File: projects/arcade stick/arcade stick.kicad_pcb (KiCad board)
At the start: 2 copper layers, 50 x 120 mm, 38 parts, among them SW1 SW_Push, SW10 SW_Push, SW11 SW_Push, SW12 SW_Push, SW13 SW_Push, SW14 SW_Push, SW15 SW_Push, SW16 SW_Push, SW2 SW_Push, SW3 SW_Push, SW4 SW_Push, SW5 SW_Push, SW6 SW_Push, SW7 SW_Push, SW8 SW_Push, SW9 SW_Push, U1 74HC165, U2 74HC165

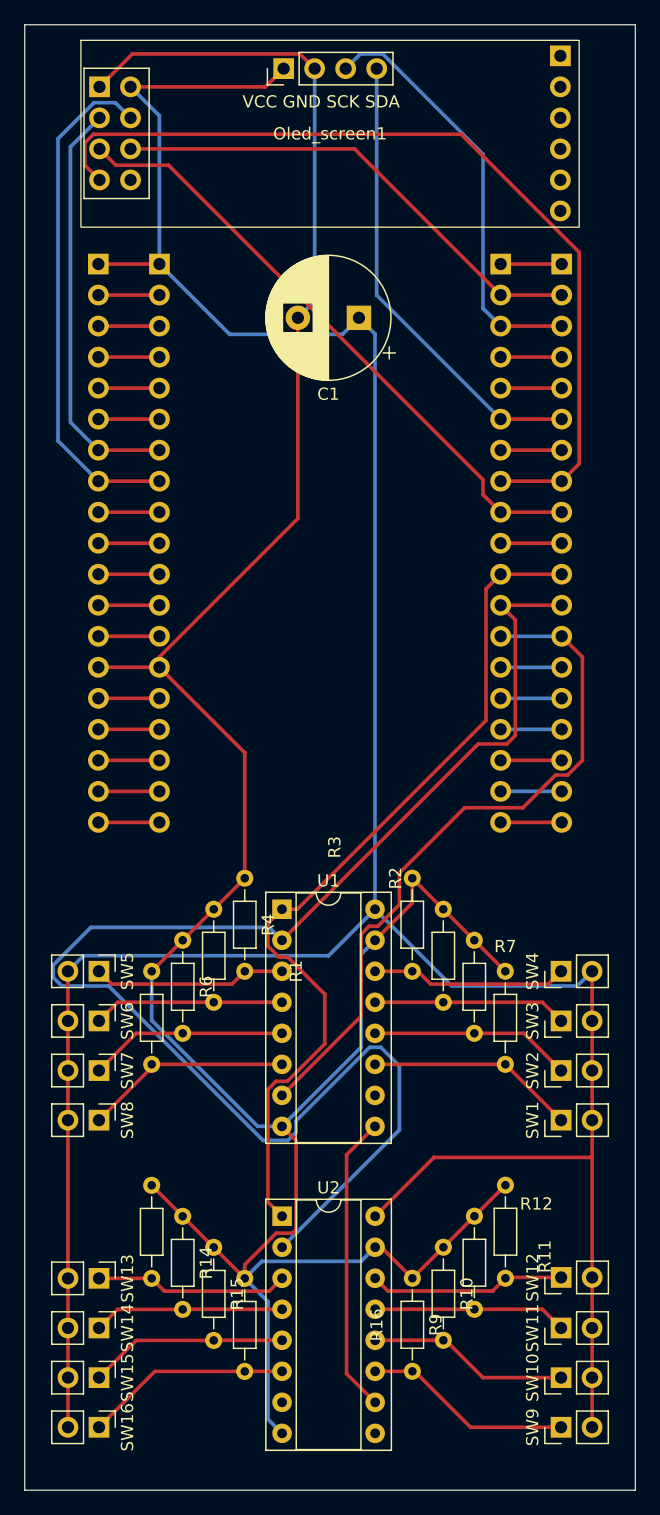
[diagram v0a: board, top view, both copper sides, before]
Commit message: update to 3.3v bat radio
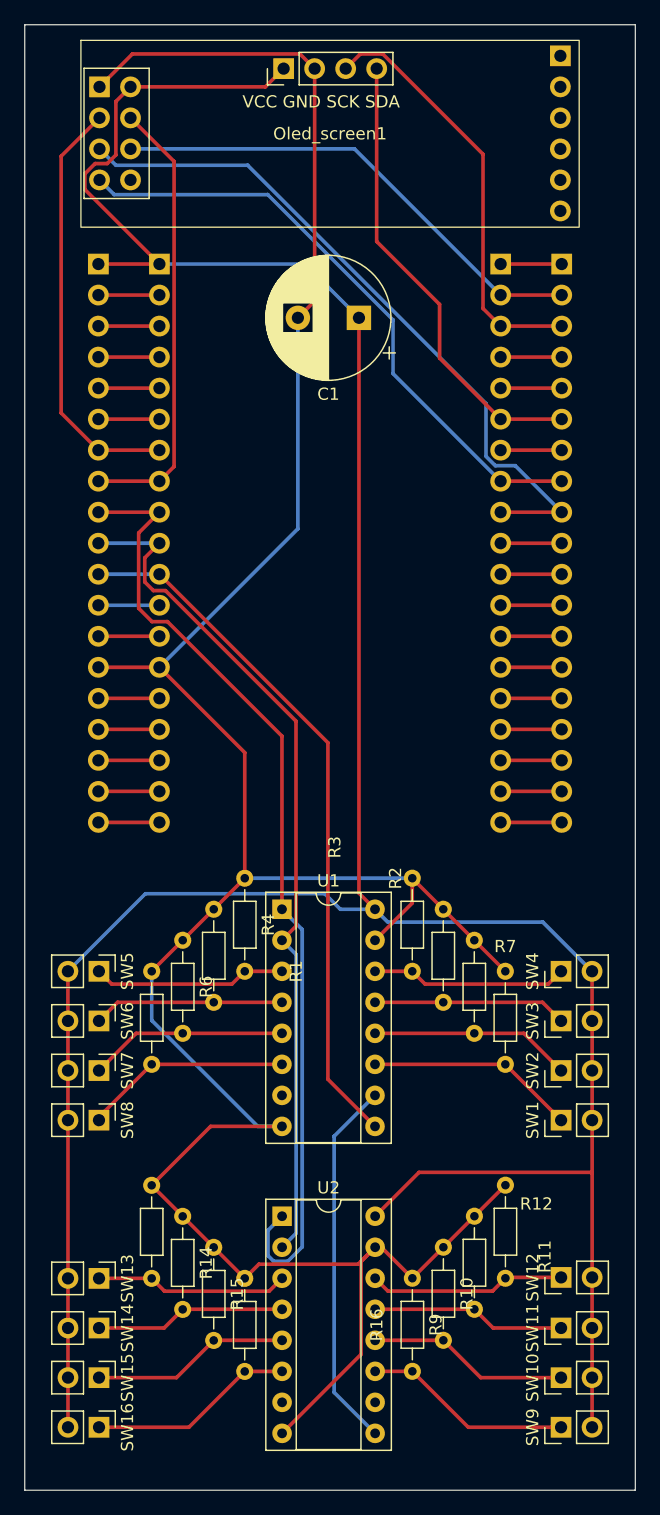
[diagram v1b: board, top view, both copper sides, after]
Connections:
- ESP32-WROOM-32U1 pad 10: unconnected-(ESP32-WROOM-32U1-26-Pad10) -> Net-(ESP32-WROOM-32U1-26)
- ESP32-WROOM-32U1 pad 11: unconnected-(ESP32-WROOM-32U1-27-Pad11) -> Net-(ESP32-WROOM-32U1-27)
- ESP32-WROOM-32U1 pad 30: Net-(ESP32-WROOM-32U1-17) -> unconnected-(ESP32-WROOM-32U1-17-Pad30)
- ESP32-WROOM-32U1 pad 31: Net-(ESP32-WROOM-32U1-16) -> unconnected-(ESP32-WROOM-32U1-16-Pad31)
- ESP32-WROOM-32U1 pad 32: Net-(ESP32-WROOM-32U1-4) -> unconnected-(ESP32-WROOM-32U1-4-Pad32)
- ESP32-WROOM-32U1 pad 9: unconnected-(ESP32-WROOM-32U1-25-Pad9) -> Net-(ESP32-WROOM-32U1-25)
- U1 pad 1: Net-(ESP32-WROOM-32U1-17) -> Net-(ESP32-WROOM-32U1-25)
- U1 pad 10: unconnected-(U1-DS-Pad10) -> Net-(U1-DS)
- U1 pad 2: Net-(ESP32-WROOM-32U1-16) -> Net-(ESP32-WROOM-32U1-26)
- U1 pad 7: Net-(ESP32-WROOM-32U1-4) -> unconnected-(U1-~{Q7}-Pad7)
- U1 pad 9: Net-(U1-Q7) -> Net-(ESP32-WROOM-32U1-27)
- U2 pad 1: Net-(ESP32-WROOM-32U1-17) -> Net-(ESP32-WROOM-32U1-25)
- U2 pad 10: Net-(U1-Q7) -> unconnected-(U2-DS-Pad10)
- U2 pad 2: Net-(ESP32-WROOM-32U1-16) -> Net-(ESP32-WROOM-32U1-26)
- U2 pad 9: unconnected-(U2-Q7-Pad9) -> Net-(U1-DS)
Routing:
- net Net-(ESP32-WROOM-32U1-16): track 120.7 -> 0.00 mm
- net Net-(ESP32-WROOM-32U1-25): track 0.00 -> 79.3 mm
- net Net-(ESP32-WROOM-32U1-17): track 71.5 -> 0.00 mm
- net Net-(ESP32-WROOM-32U1-26): track 0.00 -> 70.3 mm
- net Net-(ESP32-WROOM-32U1-27): track 0.00 -> 57.5 mm
- net Net-(ESP32-WROOM-32U1-4): track 57.3 -> 0.00 mm
- net Net-(U1-DS): track 0.00 -> 30.5 mm
- net Net-(U1-Q7): track 24.5 -> 0.00 mm
- net Net-(ESP32-WROOM-32U1-MISO/19): track 72.6 -> 50.6 mm
- net Net-(ESP32-WROOM-32U1-SCK/18): track 50.9 -> 57.7 mm
- net Net-(ESP32-WROOM-32U1-33): track 42.1 -> 36.7 mm
- net unconnected-(ESP32-WROOM-32U1-4-Pad32): track 0.00 -> 5.00 mm
- net unconnected-(ESP32-WROOM-32U1-27-Pad11): track 5.00 -> 0.00 mm
- net unconnected-(ESP32-WROOM-32U1-26-Pad10): track 5.00 -> 0.00 mm
- net unconnected-(ESP32-WROOM-32U1-25-Pad9): track 5.00 -> 0.00 mm
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
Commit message: only multi remote left
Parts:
- moved R14 0.77 mm to (106.2, 129.8)
- moved R15 0.76 mm to (108.8, 132.3)
- moved SW10 0.76 mm to (137.2, 143.0)
- moved SW11 0.76 mm to (137.2, 138.9)
- moved SW13 0.76 mm to (99.4, 134.9)
- moved SW14 0.76 mm to (99.4, 138.9)
- moved SW15 0.76 mm to (99.4, 143.0)
- moved SW16 0.76 mm to (99.4, 147.1)
- moved SW9 0.76 mm to (137.2, 147.1)
- moved R11 0.76 mm to (130.1, 129.8)
- moved R16 0.76 mm to (111.3, 134.9)
- moved R13 0.76 mm to (103.7, 127.3)
- moved U2 0.75 mm to (114.3, 129.8)
- moved R10 0.75 mm to (127.6, 132.3)
- moved R9 0.75 mm to (125.0, 134.9)
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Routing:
- net Net-(NRF1-GND): track 227.0 -> 220.8 mm
- net Net-(ESP32-WROOM-32U1-3.3v): track 246.6 -> 245.5 mm
- net Net-(U1-DS): track 30.5 -> 29.7 mm
- net Net-(ESP32-WROOM-32U1-26): track 70.3 -> 69.5 mm
- net Net-(ESP32-WROOM-32U1-25): track 79.3 -> 78.6 mm

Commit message: and to the factory it goes
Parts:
- added REF**: MountingHole_3.2mm_M3, MountingHole:MountingHole_3.2mm_M3, F.Cu at (138.8, 103.1)
- added REF**: MountingHole_3.2mm_M3, MountingHole:MountingHole_3.2mm_M3, F.Cu at (97.8, 103.1)
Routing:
- net Net-(ESP32-WROOM-32U1-25): track 78.6 -> 79.6 mm
